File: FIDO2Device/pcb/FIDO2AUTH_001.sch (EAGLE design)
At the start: 33 parts, among them CN1 TE-1734028, CN2 IF_5PIN_H, CN3 IF_3PIN, SW1 SKRPACE010, SW2 SKTADAE010, U1 MDBT50Q-P1M, U2 XC6206P332MR-G, X1 NX3215SA-32.768K

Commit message: ブレークアウト基板回路図
・汎用I/Oとして、デジタル／アナログ双方が使用できるピンを選定
・全ての配線を完了
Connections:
- new net AIN0: CN3.2, U1.P0.02/AIN0
- new net AIN1: CN3.3, U1.P0.03/AIN1
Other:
- moved on the sheet: CN3
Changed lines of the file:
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@@
 <setting verticaltext="up"/>
 </settings>
-<grid distance="0.1" unitdist="inch" unit="inch" style="lines" multiple="1" display="yes" altdistance="0.01" altunitdist="inch" altunit="inch"/>
+<grid distance="0.1" unitdist="inch" unit="inch" style="lines" multiple="1" display="no" altdistance="0.01" altunitdist="inch" altunit="inch"/>
 <layers>
 <layer number="1" name="Top" color="4" fill="1" visible="no" active="no"/>
@@
 </segment>
 </net>
+<net name="AIN0" class="0">
+<segment>
+<pinref part="U1" gate="G$1" pin="P0.02/AIN0"/>
+<wire x1="43.18" y1="86.36" x2="35.56" y2="86.36" width="0.1524" layer="91"/>
+<label x="35.56" y="86.36" size="1.778" layer="95" rot="R180" xref="yes"/>
+</segment>
+</net>
+<net name="AIN1" class="0">
+<segment>
+<pinref part="U1" gate="G$1" pin="P0.03/AIN1"/>
+<wire x1="43.18" y1="91.44" x2="35.56" y2="91.44" width="0.1524" layer="91"/>
+<label x="35.56" y="91.44" size="1.778" layer="95" rot="R180" xref="yes"/>
+<label x="35.56" y="91.44" size="1.778" layer="95" rot="R180" xref="yes"/>
+</segment>
+</net>
 </nets>
 </sheet>
@@
 <instance part="BAT1" gate="G$1" x="93.98" y="81.28"/>
 <instance part="GND18" gate="1" x="66.04" y="71.12"/>
-<instance part="CN3" gate="G$1" x="104.14" y="30.48"/>
-<instance part="GND19" gate="1" x="96.52" y="17.78"/>
+<instance part="CN3" gate="G$1" x="203.2" y="68.58"/>
+<instance part="GND19" gate="1" x="195.58" y="55.88"/>
 </instances>
 <busses>
@@
 <pinref part="CN3" gate="G$1" pin="1"/>
 <pinref part="GND19" gate="1" pin="0V"/>
-<wire x1="104.14" y1="25.4" x2="96.52" y2="25.4" width="0.1524" layer="91"/>
-<wire x1="96.52" y1="25.4" x2="96.52" y2="20.32" width="0.1524" layer="91"/>
+<wire x1="203.2" y1="63.5" x2="195.58" y2="63.5" width="0.1524" layer="91"/>
+<wire x1="195.58" y1="63.5" x2="195.58" y2="58.42" width="0.1524" layer="91"/>
 </segment>
 </net>
@@
 </segment>
 </net>
-<net name="N$1" class="0">
-<segment>
-<wire x1="73.66" y1="73.66" x2="119.38" y2="73.66" width="0.1524" layer="91"/>
-<wire x1="119.38" y1="73.66" x2="119.38" y2="55.88" width="0.1524" layer="91"/>
-<wire x1="119.38" y1="55.88" x2="73.66" y2="55.88" width="0.1524" layer="91"/>
-<wire x1="73.66" y1="55.88" x2="73.66" y2="73.66" width="0.1524" layer="91"/>
-</segment>
-</net>
 <net name="N$5" class="0">
 <segment>
@@
 </segment>
 </net>
+<net name="AIN0" class="0">
+<segment>
+<pinref part="CN3" gate="G$1" pin="2"/>
+<wire x1="203.2" y1="66.04" x2="190.5" y2="66.04" width="0.1524" layer="91"/>
+<wire x1="190.5" y1="66.04" x2="190.5" y2="71.12" width="0.1524" layer="91"/>
+<label x="190.5" y="71.12" size="1.778" layer="95" rot="R90" xref="yes"/>
+</segment>
+</net>
+<net name="AIN1" class="0">
+<segment>
+<pinref part="CN3" gate="G$1" pin="3"/>
+<wire x1="203.2" y1="68.58" x2="195.58" y2="68.58" width="0.1524" layer="91"/>
+<wire x1="195.58" y1="68.58" x2="195.58" y2="71.12" width="0.1524" layer="91"/>
+<label x="195.58" y="71.12" size="1.778" layer="95" rot="R90" xref="yes"/>
+</segment>
+</net>

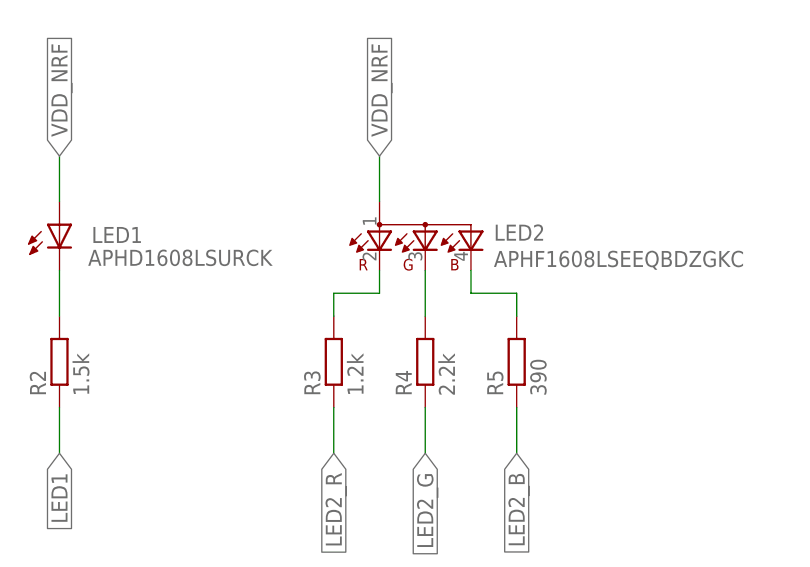
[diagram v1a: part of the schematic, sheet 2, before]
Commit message: ブレークアウト基板回路図を修正
・３色LEDの配線が間違っていたので修正
・シルクの位置等を見直し
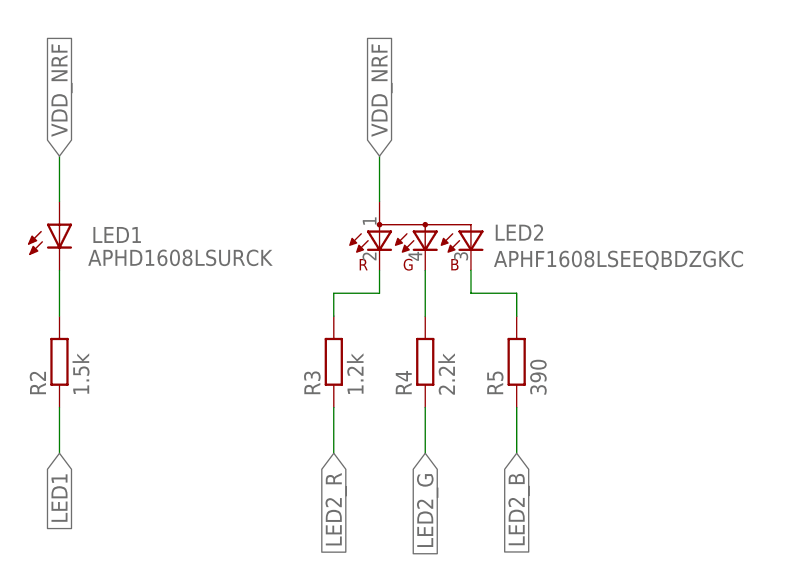
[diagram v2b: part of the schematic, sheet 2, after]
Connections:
- removed net N$10: LED2.CGREEN, R5.2
- removed net N$9: LED2.CBLUE, R4.2
- new net N$6: LED2.CGREEN, R4.2
- new net N$7: LED2.CBLUE, R5.2
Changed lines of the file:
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@@
 <setting verticaltext="up"/>
 </settings>
-<grid distance="0.1" unitdist="inch" unit="inch" style="lines" multiple="1" display="no" altdistance="0.01" altunitdist="inch" altunit="inch"/>
+<grid distance="0.1" unitdist="inch" unit="inch" style="lines" multiple="1" display="yes" altdistance="0.01" altunitdist="inch" altunit="inch"/>
 <layers>
 <layer number="1" name="Top" color="4" fill="1" visible="no" active="no"/>
@@
 </segment>
 </net>
-<net name="N$8" class="0">
-<segment>
-<pinref part="LED2" gate="G$1" pin="CRED"/>
-<wire x1="91.44" y1="55.88" x2="91.44" y2="53.34" width="0.1524" layer="91"/>
-<wire x1="91.44" y1="53.34" x2="86.36" y2="53.34" width="0.1524" layer="91"/>
-<pinref part="R3" gate="G$1" pin="2"/>
-<wire x1="86.36" y1="53.34" x2="86.36" y2="50.8" width="0.1524" layer="91"/>
-</segment>
-</net>
-<net name="N$9" class="0">
-<segment>
-<pinref part="LED2" gate="G$1" pin="CBLUE"/>
-<pinref part="R4" gate="G$1" pin="2"/>
-<wire x1="96.52" y1="55.88" x2="96.52" y2="50.8" width="0.1524" layer="91"/>
-</segment>
-</net>
-<net name="N$10" class="0">
-<segment>
-<pinref part="LED2" gate="G$1" pin="CGREEN"/>
-<wire x1="101.6" y1="55.88" x2="101.6" y2="53.34" width="0.1524" layer="91"/>
-<wire x1="101.6" y1="53.34" x2="106.68" y2="53.34" width="0.1524" layer="91"/>
-<pinref part="R5" gate="G$1" pin="2"/>
-<wire x1="106.68" y1="53.34" x2="106.68" y2="50.8" width="0.1524" layer="91"/>
-</segment>
-</net>
 <net name="N$11" class="0">
 <segment>
@@
 </segment>
 </net>
+<net name="N$1" class="0">
+<segment>
+<pinref part="R3" gate="G$1" pin="2"/>
+<wire x1="86.36" y1="50.8" x2="86.36" y2="53.34" width="0.1524" layer="91"/>
+<wire x1="86.36" y1="53.34" x2="91.44" y2="53.34" width="0.1524" layer="91"/>
+<pinref part="LED2" gate="G$1" pin="CRED"/>
+<wire x1="91.44" y1="53.34" x2="91.44" y2="55.88" width="0.1524" layer="91"/>
+</segment>
+</net>
+<net name="N$6" class="0">
+<segment>
+<pinref part="LED2" gate="G$1" pin="CGREEN"/>
+<pinref part="R4" gate="G$1" pin="2"/>
+<wire x1="96.52" y1="55.88" x2="96.52" y2="50.8" width="0.1524" layer="91"/>
+</segment>
+</net>
+<net name="N$7" class="0">
+<segment>
+<pinref part="LED2" gate="G$1" pin="CBLUE"/>
+<wire x1="101.6" y1="55.88" x2="101.6" y2="53.34" width="0.1524" layer="91"/>
+<pinref part="R5" gate="G$1" pin="2"/>
+<wire x1="101.6" y1="53.34" x2="106.68" y2="53.34" width="0.1524" layer="91"/>
+<wire x1="106.68" y1="53.34" x2="106.68" y2="50.8" width="0.1524" layer="91"/>
+</segment>
+</net>
